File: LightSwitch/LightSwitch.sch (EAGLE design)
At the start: 27 parts, among them Q2 TIP120, Y1 16MHz

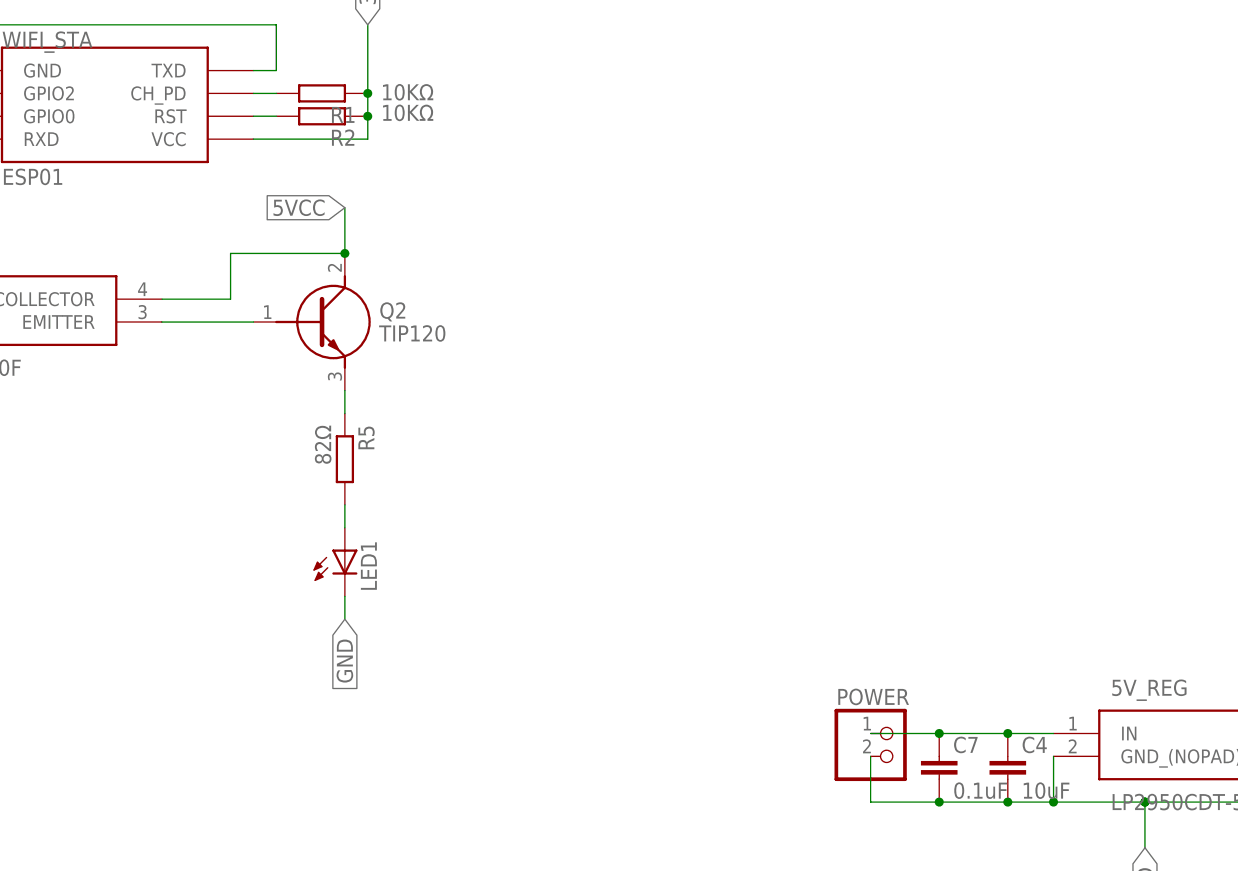
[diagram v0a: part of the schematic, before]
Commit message: Add resistors and voltage regulator as well as pinheader
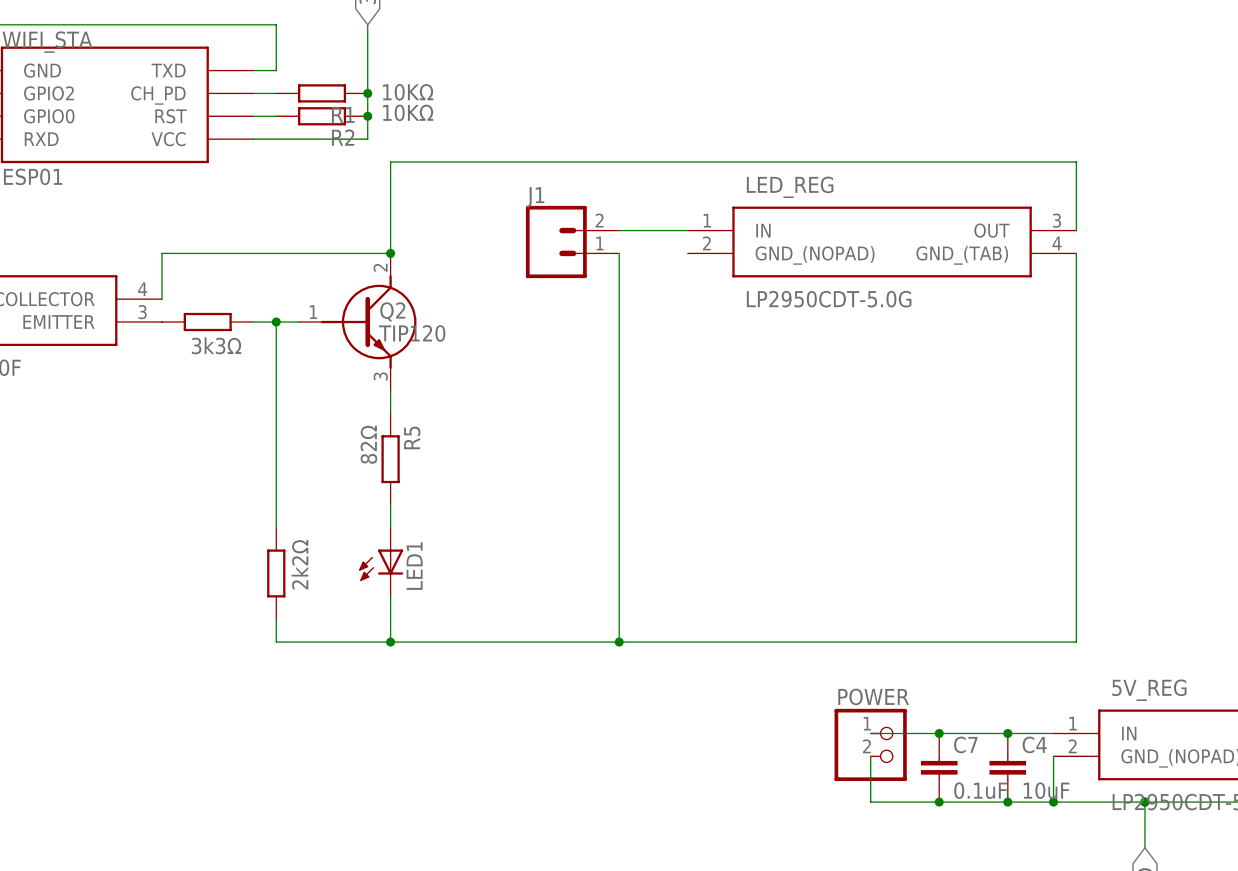
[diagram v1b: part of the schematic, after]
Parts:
- added J1: (no value), SparkFun-Connectors:CONN_025MM
- added LED_REG: LP2950CDT-5.0G, LP2950CDT-5.0G:LP2950CDT-5.0G
- added R7: 3k3Ω, eagle-ltspice:RR1210
- added R8: 2k2Ω, eagle-ltspice:RR1210
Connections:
- new net LED_GND: J1.1, LED1.C, LED_REG.GND_(TAB), R8.2
- new net LED_VCC: LED_REG.OUT, OPTO.COLLECTOR, Q2.C
- new net LED_VIN: J1.2, LED_REG.IN
- new net N$1: OPTO.EMITTER, R7.2
- net 5VCC: no longer OPTO.COLLECTOR, Q2.C
- net GND: no longer LED1.C
- net OPTO_EMITTER: now also R7.1, R8.1; no longer OPTO.EMITTER
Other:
- moved on the sheet: LED1, Q2, R5
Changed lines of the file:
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@@
 <layer number="230" name="230bmp" color="7" fill="1" visible="yes" active="yes"/>
 <layer number="231" name="231bmp" color="7" fill="1" visible="yes" active="yes"/>
+<layer number="232" name="Eagle3D_PG2" color="7" fill="1" visible="yes" active="yes"/>
+<layer number="233" name="Eagle3D_PG3" color="7" fill="1" visible="yes" active="yes"/>
 <layer number="248" name="Housing" color="7" fill="1" visible="yes" active="yes"/>
 <layer number="249" name="Edge" color="7" fill="1" visible="yes" active="yes"/>
@@
 <part name="R5" library="eagle-ltspice" library_urn="urn:adsk.eagle:library:217" deviceset="R" device="R1210" package3d_urn="urn:adsk.eagle:package:13299/1" value="82Ω"/>
 <part name="LED1" library="eagle-ltspice" library_urn="urn:adsk.eagle:library:217" deviceset="LED_E" device="LD260" package3d_urn="urn:adsk.eagle:package:13313/1"/>
+<part name="R7" library="eagle-ltspice" library_urn="urn:adsk.eagle:library:217" deviceset="R" device="R1210" package3d_urn="urn:adsk.eagle:package:13299/1" value="3k3Ω"/>
+<part name="LED_REG" library="LP2950CDT-5.0G" deviceset="LP2950CDT-5.0G" device=""/>
+<part name="J1" library="SparkFun-Connectors" library_urn="urn:adsk.eagle:library:513" deviceset="CONN_02" device="5MM" package3d_urn="urn:adsk.eagle:package:38044/1"/>
+<part name="R8" library="eagle-ltspice" library_urn="urn:adsk.eagle:library:217" deviceset="R" device="R1210" package3d_urn="urn:adsk.eagle:package:13299/1" value="2k2Ω"/>
 </parts>
 <sheets>
@@
 <attribute name="VALUE" x="52.07" y="23.622" size="1.778" layer="96" rot="R180"/>
 </instance>
-<instance part="Q2" gate="G$1" x="109.22" y="20.32" smashed="yes">
+<instance part="Q2" gate="G$1" x="114.3" y="20.32" smashed="yes">
 <attribute name="NAME" x="123.19" y="21.59" size="1.778" layer="95" align="center-left"/>
 <attribute name="VALUE" x="123.19" y="19.05" size="1.778" layer="96" align="center-left"/>
 </instance>
-<instance part="R5" gate="G$1" x="119.38" y="5.08" smashed="yes" rot="R270">
-<attribute name="NAME" x="120.8786" y="8.89" size="1.778" layer="95" rot="R270"/>
-<attribute name="VALUE" x="116.078" y="8.89" size="1.778" layer="96" rot="R270"/>
-</instance>
-<instance part="LED1" gate="G$1" x="119.38" y="-5.08" smashed="yes">
-<attribute name="NAME" x="122.936" y="-9.652" size="1.778" layer="95" rot="R90"/>
-<attribute name="VALUE" x="125.095" y="-9.652" size="1.778" layer="96" rot="R90"/>
+<instance part="R5" gate="G$1" x="124.46" y="5.08" smashed="yes" rot="R270">
+<attribute name="NAME" x="125.9586" y="8.89" size="1.778" layer="95" rot="R270"/>
+<attribute name="VALUE" x="121.158" y="8.89" size="1.778" layer="96" rot="R270"/>
+</instance>
+<instance part="LED1" gate="G$1" x="124.46" y="-5.08" smashed="yes">
+<attribute name="NAME" x="128.016" y="-9.652" size="1.778" layer="95" rot="R90"/>
+<attribute name="VALUE" x="130.175" y="-9.652" size="1.778" layer="96" rot="R90"/>
+</instance>
+<instance part="R7" gate="G$1" x="104.14" y="20.32" smashed="yes" rot="R180">
+<attribute name="VALUE" x="107.95" y="18.542" size="1.778" layer="96" rot="R180"/>
+</instance>
+<instance part="LED_REG" gate="G$1" x="157.48" y="30.48" smashed="yes">
+<attribute name="NAME" x="163.83" y="35.56" size="1.778" layer="95" align="center-left"/>
+<attribute name="VALUE" x="163.83" y="22.86" size="1.778" layer="96" align="center-left"/>
+</instance>
+<instance part="J1" gate="G$1" x="142.24" y="27.94" smashed="yes">
+<attribute name="VALUE" x="139.7" y="23.114" size="1.778" layer="96" font="vector"/>
+<attribute name="NAME" x="139.7" y="33.528" size="1.778" layer="95" font="vector"/>
+</instance>
+<instance part="R8" gate="G$1" x="111.76" y="-7.62" smashed="yes" rot="R270">
+<attribute name="VALUE" x="113.538" y="-3.81" size="1.778" layer="96" rot="R270"/>
 </instance>
 </instances>
@@
 <junction x="30.48" y="22.86"/>
 </segment>
-<segment>
-<pinref part="LED1" gate="G$1" pin="C"/>
-<wire x1="119.38" y1="-10.16" x2="119.38" y2="-12.7" width="0.1524" layer="91"/>
-<label x="119.38" y="-12.7" size="1.778" layer="95" rot="R270" xref="yes"/>
-</segment>
 </net>
 <net name="3VCC" class="1">
@@
 <pinref part="3V_REG" gate="G$1" pin="IN"/>
 </segment>
-<segment>
-<pinref part="Q2" gate="G$1" pin="C"/>
-<wire x1="119.38" y1="33.02" x2="119.38" y2="27.94" width="0.1524" layer="91"/>
-<wire x1="119.38" y1="27.94" x2="106.68" y2="27.94" width="0.1524" layer="91"/>
-<junction x="119.38" y="27.94"/>
-<wire x1="106.68" y1="27.94" x2="106.68" y2="22.86" width="0.1524" layer="91"/>
-<pinref part="OPTO" gate="G$1" pin="COLLECTOR"/>
-<wire x1="106.68" y1="22.86" x2="99.06" y2="22.86" width="0.1524" layer="91"/>
-<label x="119.38" y="33.02" size="1.778" layer="95" rot="R180" xref="yes"/>
-</segment>
 </net>
 <net name="STA_TXD" class="0">
@@
 <net name="OPTO_EMITTER" class="0">
 <segment>
-<pinref part="OPTO" gate="G$1" pin="EMITTER"/>
 <pinref part="Q2" gate="G$1" pin="B"/>
-<wire x1="99.06" y1="20.32" x2="109.22" y2="20.32" width="0.1524" layer="91"/>
+<pinref part="R7" gate="G$1" pin="1"/>
+<wire x1="114.3" y1="20.32" x2="111.76" y2="20.32" width="0.1524" layer="91"/>
+<pinref part="R8" gate="G$1" pin="1"/>
+<wire x1="111.76" y1="20.32" x2="109.22" y2="20.32" width="0.1524" layer="91"/>
+<wire x1="111.76" y1="-2.54" x2="111.76" y2="20.32" width="0.1524" layer="91"/>
+<junction x="111.76" y="20.32"/>
 </segment>
 </net>
@@
 <pinref part="R5" gate="G$1" pin="1"/>
 <pinref part="Q2" gate="G$1" pin="E"/>
-<wire x1="119.38" y1="10.16" x2="119.38" y2="12.7" width="0.1524" layer="91"/>
+<wire x1="124.46" y1="10.16" x2="124.46" y2="12.7" width="0.1524" layer="91"/>
 </segment>
 </net>
@@
 <pinref part="R5" gate="G$1" pin="2"/>
 <pinref part="LED1" gate="G$1" pin="A"/>
-<wire x1="119.38" y1="-2.54" x2="119.38" y2="0" width="0.1524" layer="91"/>
+<wire x1="124.46" y1="-2.54" x2="124.46" y2="0" width="0.1524" layer="91"/>
+</segment>
+</net>
+<net name="N$1" class="0">
+<segment>
+<pinref part="OPTO" gate="G$1" pin="EMITTER"/>
+<pinref part="R7" gate="G$1" pin="2"/>
+</segment>
+</net>
+<net name="LED_VIN" class="0">
+<segment>
+<pinref part="J1" gate="G$1" pin="2"/>
+<pinref part="LED_REG" gate="G$1" pin="IN"/>
+<wire x1="149.86" y1="30.48" x2="157.48" y2="30.48" width="0.1524" layer="91"/>
+</segment>
+</net>
+<net name="LED_GND" class="1">
+<segment>
+<pinref part="LED1" gate="G$1" pin="C"/>
+<wire x1="149.86" y1="-15.24" x2="124.46" y2="-15.24" width="0.1524" layer="91"/>
+<wire x1="124.46" y1="-15.24" x2="124.46" y2="-10.16" width="0.1524" layer="91"/>
+<pinref part="J1" gate="G$1" pin="1"/>
+<wire x1="149.86" y1="27.94" x2="149.86" y2="-15.24" width="0.1524" layer="91"/>
+<junction x="149.86" y="-15.24"/>
+<pinref part="LED_REG" gate="G$1" pin="GND_(TAB)"/>
+<wire x1="149.86" y1="-15.24" x2="200.66" y2="-15.24" width="0.1524" layer="91"/>
+<wire x1="200.66" y1="-15.24" x2="200.66" y2="27.94" width="0.1524" layer="91"/>
+<pinref part="R8" gate="G$1" pin="2"/>
+<wire x1="124.46" y1="-15.24" x2="111.76" y2="-15.24" width="0.1524" layer="91"/>
+<wire x1="111.76" y1="-15.24" x2="111.76" y2="-12.7" width="0.1524" layer="91"/>
+<junction x="124.46" y="-15.24"/>
+</segment>
+</net>
+<net name="LED_VCC" class="1">
+<segment>
+<pinref part="LED_REG" gate="G$1" pin="OUT"/>
+<wire x1="200.66" y1="30.48" x2="200.66" y2="38.1" width="0.1524" layer="91"/>
+<pinref part="Q2" gate="G$1" pin="C"/>
+<wire x1="200.66" y1="38.1" x2="124.46" y2="38.1" width="0.1524" layer="91"/>
+<wire x1="124.46" y1="38.1" x2="124.46" y2="27.94" width="0.1524" layer="91"/>
+<wire x1="124.46" y1="27.94" x2="99.06" y2="27.94" width="0.1524" layer="91"/>
+<junction x="124.46" y="27.94"/>
+<pinref part="OPTO" gate="G$1" pin="COLLECTOR"/>
+<wire x1="99.06" y1="27.94" x2="99.06" y2="22.86" width="0.1524" layer="91"/>
 </segment>
 </net>
@@
 </sheet>
 </sheets>
-<errors>
-</errors>
 </schematic>
 </drawing>

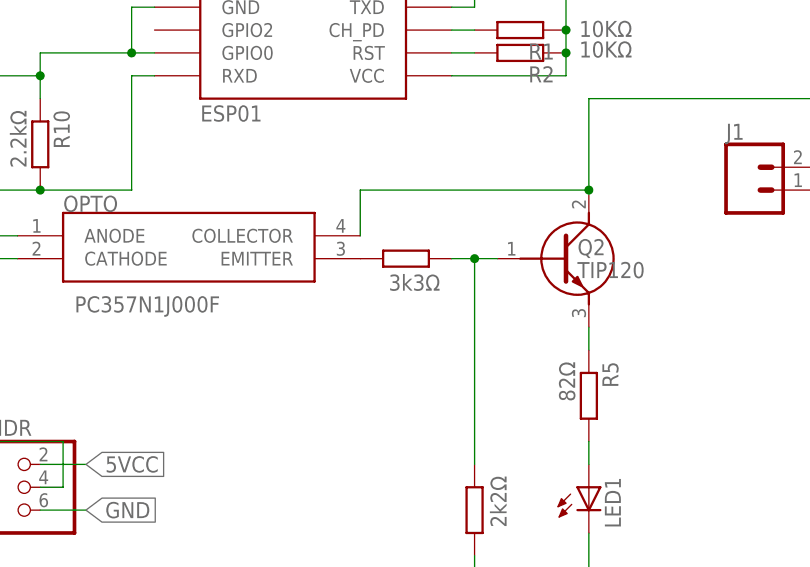
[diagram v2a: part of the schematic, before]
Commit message: wifitracker fix
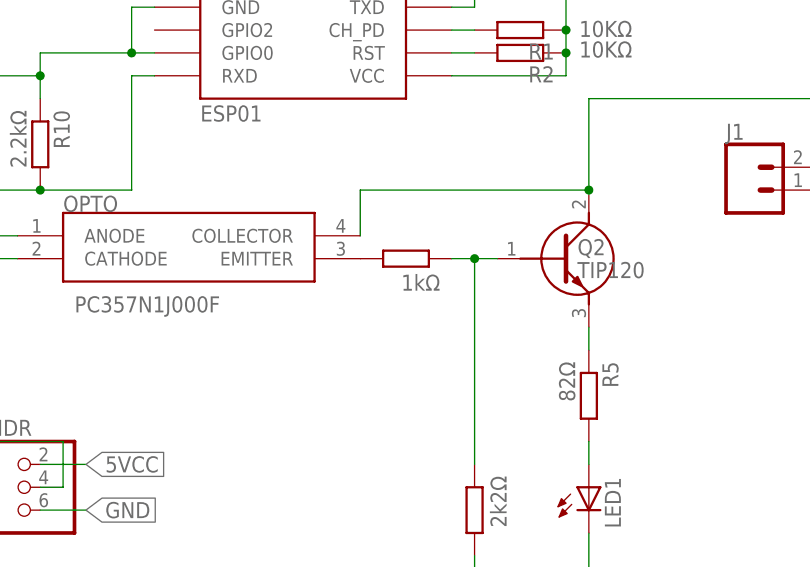
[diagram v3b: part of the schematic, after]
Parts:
- R7: value 3k3Ω -> 1kΩ
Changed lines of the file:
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@@
 <part name="R5" library="eagle-ltspice" library_urn="urn:adsk.eagle:library:217" deviceset="R" device="R1210" package3d_urn="urn:adsk.eagle:package:13299/1" value="82Ω"/>
 <part name="LED1" library="eagle-ltspice" library_urn="urn:adsk.eagle:library:217" deviceset="LED_E" device="LD260" package3d_urn="urn:adsk.eagle:package:13313/1"/>
-<part name="R7" library="eagle-ltspice" library_urn="urn:adsk.eagle:library:217" deviceset="R" device="R1210" package3d_urn="urn:adsk.eagle:package:13299/1" value="3k3Ω"/>
+<part name="R7" library="eagle-ltspice" library_urn="urn:adsk.eagle:library:217" deviceset="R" device="R1210" package3d_urn="urn:adsk.eagle:package:13299/1" value="1kΩ"/>
 <part name="LED_REG" library="LP2950CDT-5.0G" deviceset="LP2950CDT-5.0G" device=""/>
 <part name="J1" library="SparkFun-Connectors" library_urn="urn:adsk.eagle:library:513" deviceset="CONN_02" device="5MM" package3d_urn="urn:adsk.eagle:package:38044/1"/>
